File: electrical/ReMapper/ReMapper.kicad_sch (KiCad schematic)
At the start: 42 parts, among them J1 ESP_UART0, J2 I2C Display, J3 USB_IN, J4 USB_OUT, J5 Button GND Pad, J9 Button Socket, U1 SPX1117M3-L-3-3/TR, U2 W25Q128JVE, U3 ESP32-S3-WROOM-1-N8R8, U4 RP2040, U5 W25Q128JVE, Y1 12MHZ

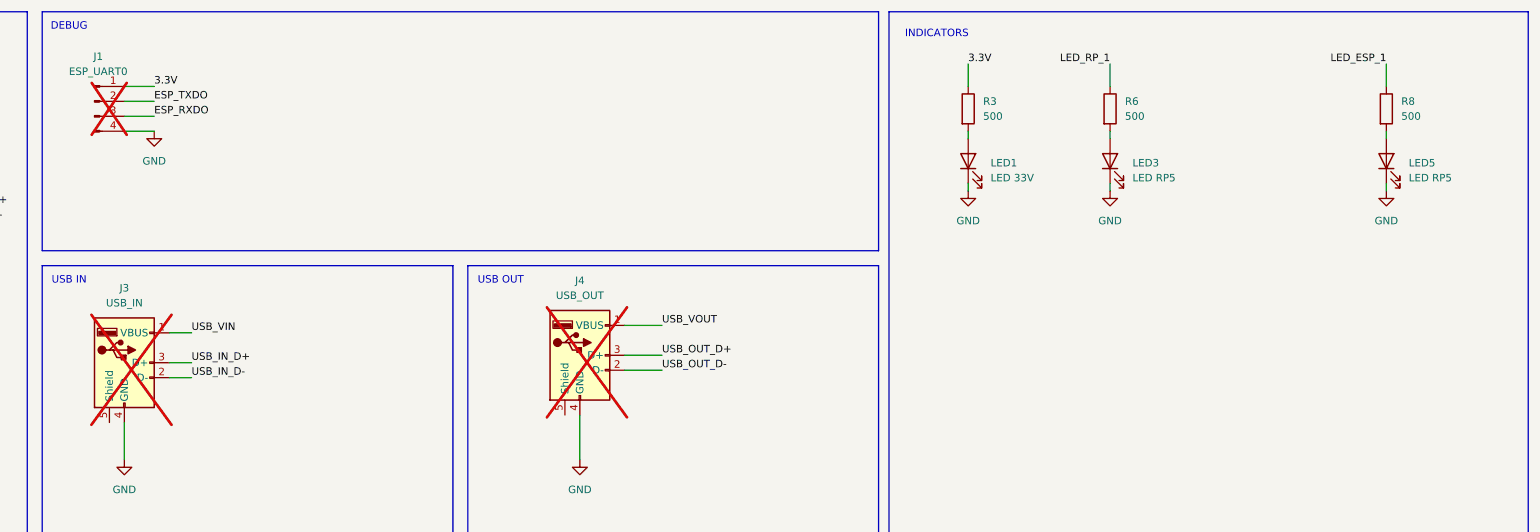
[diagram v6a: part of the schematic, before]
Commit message: It ssems too small, I need some space for trace highways
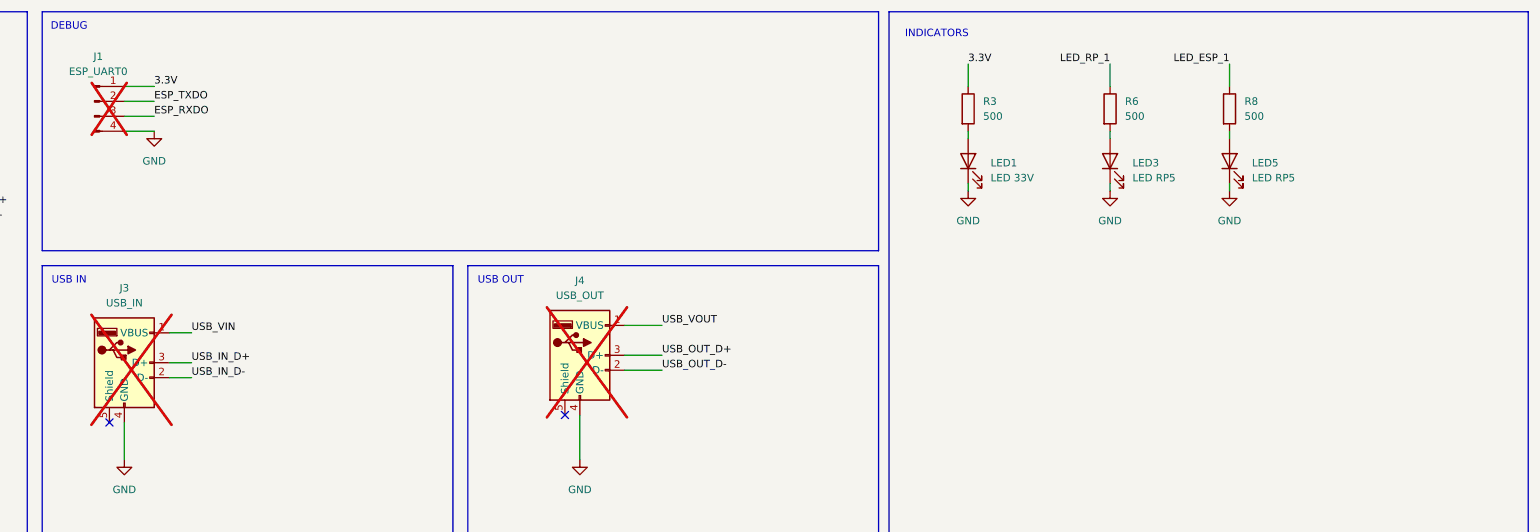
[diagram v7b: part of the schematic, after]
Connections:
- no-connect marks 45 -> 47
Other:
- moved on the sheet: LED5, R8
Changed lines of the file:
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@@
 	)
 	(no_connect
+		(at 165.1 86.36)
+	)
+	(no_connect
 		(at 204.47 212.09)
 	)
@@
 	)
 	(no_connect
+		(at 242.57 85.09)
+	)
+	(no_connect
 		(at 158.75 146.05)
 	)
@@
 	(wire
 		(pts
-			(xy 382.27 45.72) (xy 382.27 46.99)
+			(xy 355.6 45.72) (xy 355.6 46.99)
 		)
 		(stroke
@@
 	(wire
 		(pts
-			(xy 382.27 25.4) (xy 382.27 29.21)
+			(xy 355.6 25.4) (xy 355.6 29.21)
 		)
 		(stroke
@@
 	(wire
 		(pts
-			(xy 382.27 36.83) (xy 382.27 38.1)
+			(xy 355.6 36.83) (xy 355.6 38.1)
 		)
 		(stroke
@@
 	)
 	(label "LED_ESP_1"
-		(at 382.27 25.4 180)
+		(at 355.6 25.4 180)
 		(effects
 			(font
@@
 	(symbol
 		(lib_id "Device:R")
-		(at 382.27 33.02 0)
+		(at 355.6 33.02 0)
 		(unit 1)
 		(exclude_from_sim no)
@@
 		(dnp no)
 		(property "Reference" "R8"
-			(at 384.81 31.7499 0)
+			(at 358.14 31.7499 0)
 			(effects
 				(font
@@
 		)
 		(property "Value" "500"
-			(at 384.81 34.2899 0)
+			(at 358.14 34.2899 0)
 			(effects
 				(font
@@
 		)
 		(property "Footprint" "Resistor_SMD:R_0603_1608Metric"
-			(at 380.492 33.02 90)
+			(at 353.822 33.02 90)
 			(effects
 				(font
@@
 		)
 		(property "Datasheet" "~"
-			(at 382.27 33.02 0)
+			(at 355.6 33.02 0)
 			(effects
 				(font
@@
 		)
 		(property "Description" "Resistor"
-			(at 382.27 33.02 0)
+			(at 355.6 33.02 0)
 			(effects
 				(font
@@
 		)
 		(property "LCSC Part" "C860931"
-			(at 382.27 33.02 0)
+			(at 355.6 33.02 0)
 			(effects
 				(font
@@
 		)
 		(property "SNAPEDA_PACKAGE_ID" ""
-			(at 382.27 33.02 0)
+			(at 355.6 33.02 0)
 			(effects
 				(font
@@
 	(symbol
 		(lib_id "power:GND")
-		(at 382.27 46.99 0)
+		(at 355.6 46.99 0)
 		(unit 1)
 		(exclude_from_sim no)
@@
 		(fields_autoplaced yes)
 		(property "Reference" "#PWR034"
-			(at 382.27 53.34 0)
+			(at 355.6 53.34 0)
 			(effects
 				(font
@@
 		)
 		(property "Value" "GND"
-			(at 382.27 52.07 0)
+			(at 355.6 52.07 0)
 			(effects
 				(font
@@
 		)
 		(property "Footprint" ""
-			(at 382.27 46.99 0)
+			(at 355.6 46.99 0)
 			(effects
 				(font
@@
 		)
 		(property "Datasheet" ""
-			(at 382.27 46.99 0)
+			(at 355.6 46.99 0)
 			(effects
 				(font
@@
 		)
 		(property "Description" "Power symbol creates a global label with name \"GND\" , ground"
-			(at 382.27 46.99 0)
+			(at 355.6 46.99 0)
 			(effects
 				(font
@@
 	(symbol
 		(lib_id "Device:LED")
-		(at 382.27 41.91 90)
+		(at 355.6 41.91 90)
 		(unit 1)
 		(exclude_from_sim no)
@@
 		(fields_autoplaced yes)
 		(property "Reference" "LED5"
-			(at 386.08 42.2274 90)
+			(at 359.41 42.2274 90)
 			(effects
 				(font
@@
 		)
 		(property "Value" "LED RP5"
-			(at 386.08 44.7674 90)
+			(at 359.41 44.7674 90)
 			(effects
 				(font
@@
 		)
 		(property "Footprint" "LED_SMD:LED_0603_1608Metric"
-			(at 382.27 41.91 0)
+			(at 355.6 41.91 0)
 			(effects
 				(font
@@
 		)
 		(property "Datasheet" "~"
-			(at 382.27 41.91 0)
+			(at 355.6 41.91 0)
 			(effects
 				(font
@@
 		)
 		(property "Description" "Light emitting diode"
-			(at 382.27 41.91 0)
+			(at 355.6 41.91 0)
 			(effects
 				(font
@@
 		)
 		(property "Sim.Pins" "1=K 2=A"
-			(at 382.27 41.91 0)
+			(at 355.6 41.91 0)
 			(effects
 				(font
@@
 		)
 		(property "LCSC Part" "C965807"
-			(at 382.27 41.91 90)
+			(at 355.6 41.91 90)
 			(effects
 				(font
@@
 		)
 		(property "SNAPEDA_PACKAGE_ID" ""
-			(at 382.27 41.91 90)
+			(at 355.6 41.91 90)
 			(effects
 				(font

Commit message: working on fab
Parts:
- D1, D2, D3, D4: LCSC Part SOD523 -> C5199159
- J5, J9: now not fitted; now left out of the parts list
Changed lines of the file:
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@@
 			)
 		)
-		(property "LCSC Part" "SOD523"
+		(property "LCSC Part" "C5199159"
 			(at 127 57.15 90)
 			(effects
@@
 			)
 		)
-		(property "LCSC Part" "SOD523"
+		(property "LCSC Part" "C5199159"
 			(at 130.81 57.15 90)
 			(effects
@@
 		(unit 1)
 		(exclude_from_sim no)
-		(in_bom yes)
+		(in_bom no)
 		(on_board yes)
-		(dnp no)
+		(dnp yes)
 		(fields_autoplaced yes)
 		(property "Reference" "J5"
@@
 		(unit 1)
 		(exclude_from_sim no)
-		(in_bom yes)
+		(in_bom no)
 		(on_board yes)
-		(dnp no)
+		(dnp yes)
 		(fields_autoplaced yes)
 		(property "Reference" "J9"
@@
 			)
 		)
-		(property "LCSC Part" "SOD523"
+		(property "LCSC Part" "C5199159"
 			(at 66.04 255.27 90)
 			(effects
@@
 			)
 		)
-		(property "LCSC Part" "SOD523"
+		(property "LCSC Part" "C5199159"
 			(at 69.85 255.27 90)
 			(effects
